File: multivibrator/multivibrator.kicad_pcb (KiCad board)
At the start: 2 copper layers, 11 parts, among them J1 Conn_01x02_Female, Q1 Q_NPN_BCE, Q2 Q_NPN_BCE

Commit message: improvement
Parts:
- J1: footprint Battery:BatteryHolder_Bulgin_BX0036_1xC -> Connector_PinHeader_2.54mm:PinHeader_1x02_P2.54mm_Vertical
- Q1, Q2: footprint Package_TO_SOT_THT:TO-92_HandSolder -> Package_TO_SOT_SMD:TSOT-23
- R1, R2, R3, R4: footprint Resistor_SMD:R_0201_0603Metric -> Resistor_SMD:R_1206_3216Metric
- moved J1 65.0 mm to (160.0, 88.9), turned to 0 degrees
- moved Q2 37.1 mm to (144.8, 96.5), turned to 90 degrees
- moved Q1 32.4 mm to (153.7, 96.5), turned to 270 degrees
- moved R4 31.0 mm to (151.1, 86.4), turned to 270 degrees
- moved C2 27.5 mm to (153.3, 91.4)
- moved D2 27.0 mm to (153.7, 82.5), turned to 90 degrees
- moved C1 25.8 mm to (145.7, 91.4)
- moved R1 25.0 mm to (143.5, 86.4), turned to 270 degrees
- moved R3 25.0 mm to (154.9, 86.4), turned to 270 degrees
- moved D1 24.5 mm to (145.8, 82.9), turned to 270 degrees
- moved R2 24.3 mm to (147.3, 86.4), turned to 270 degrees
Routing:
- net Net-(J1-Pad2): track 0.00 -> 52.4 mm
- net Net-(D1-Pad2): track 0.00 -> 28.2 mm
- net Net-(C1-Pad2): track 0.00 -> 24.8 mm
- net Net-(C2-Pad1): track 0.00 -> 14.2 mm
- net Net-(C1-Pad1): track 0.00 -> 12.3 mm
- net Net-(C2-Pad2): track 0.00 -> 8.85 mm
- net Net-(D1-Pad1): track 0.00 -> 3.68 mm
- net Net-(D2-Pad1): track 0.00 -> 3.41 mm
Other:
- rule pad_to_mask_clearance: 0.2 -> 0

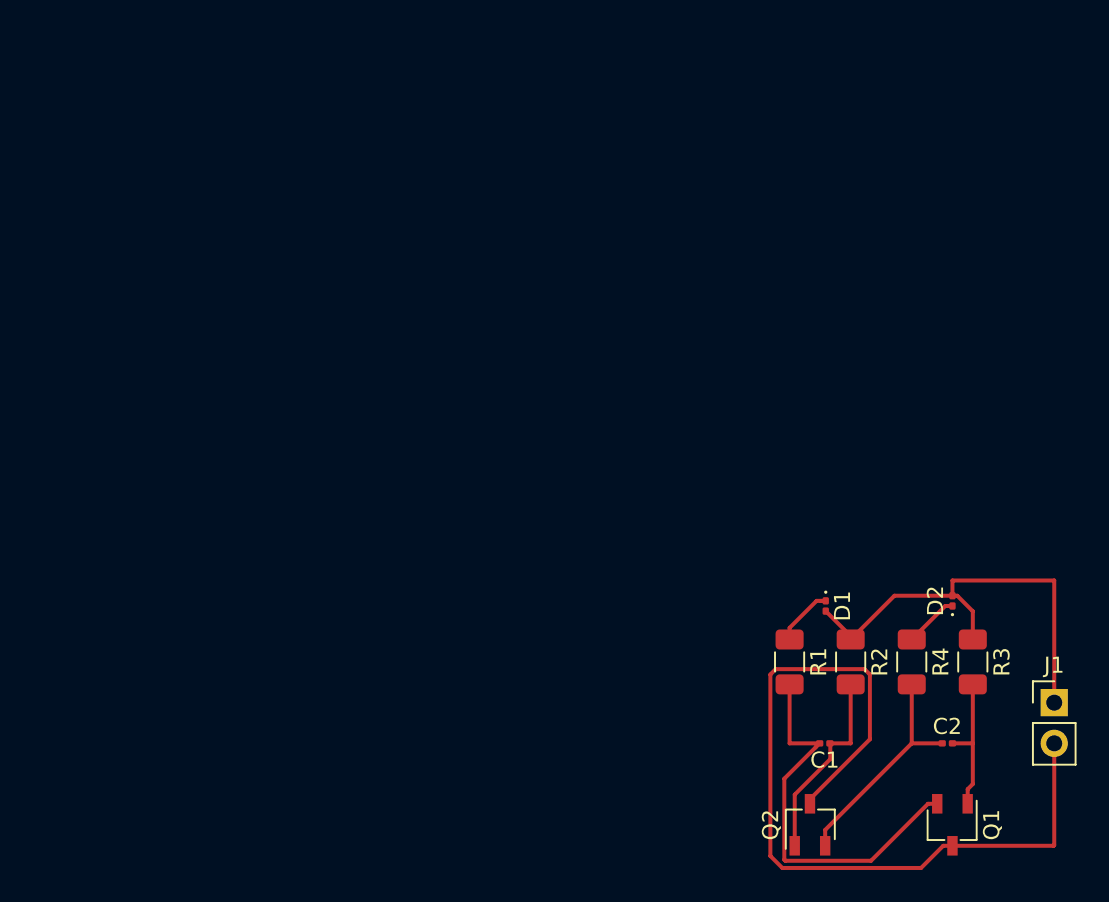
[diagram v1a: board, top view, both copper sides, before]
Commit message: review fixes, ready for print
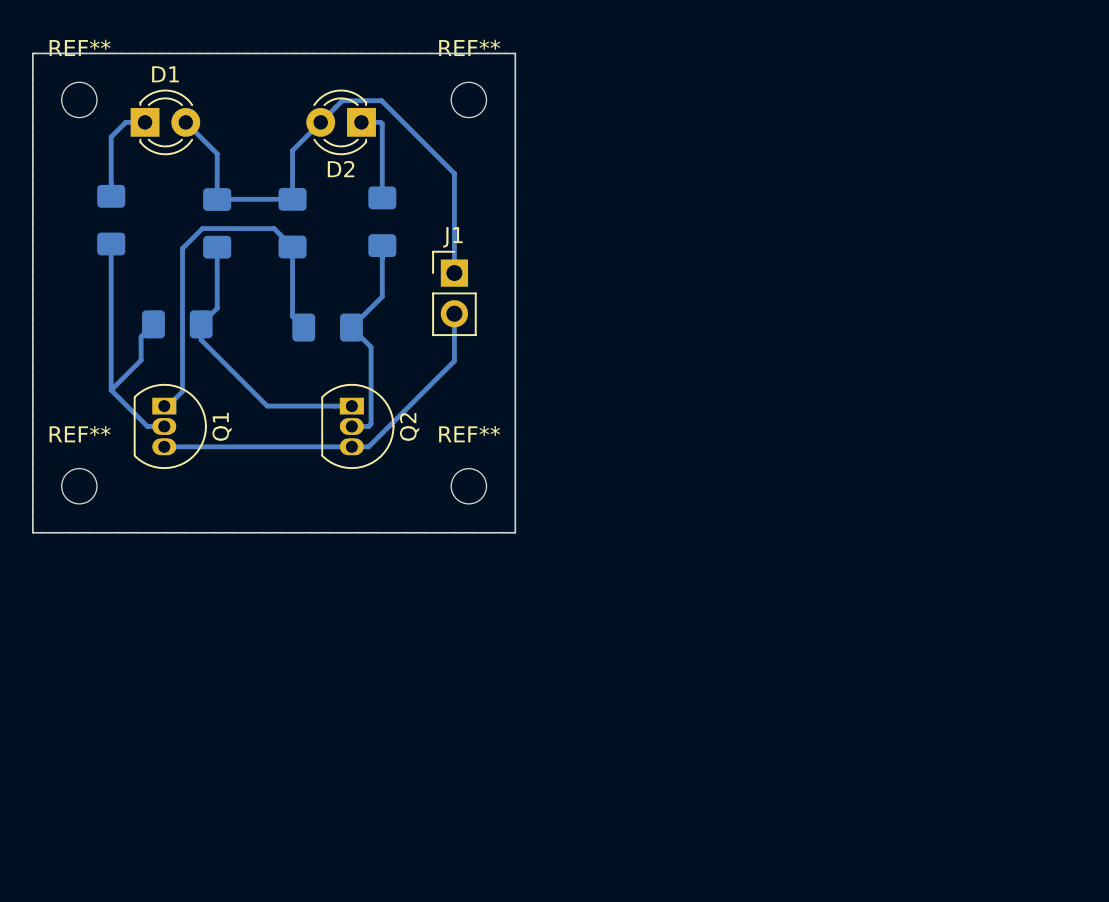
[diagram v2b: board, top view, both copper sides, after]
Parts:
- added REF**: MountingHole_2.2mm_M2, MountingHole:MountingHole_2.2mm_M2, F.Cu at (123.5, 51.3)
- added REF**: MountingHole_2.2mm_M2, MountingHole:MountingHole_2.2mm_M2, F.Cu at (99.2, 51.3)
- added REF**: MountingHole_2.2mm_M2, MountingHole:MountingHole_2.2mm_M2, F.Cu at (99.2, 75.4)
- added REF**: MountingHole_2.2mm_M2, MountingHole:MountingHole_2.2mm_M2, F.Cu at (123.5, 75.4)
- C1, C2: footprint Capacitor_SMD:C_0201_0603Metric -> Capacitor_SMD:C_1206_3216Metric_Pad1.42x1.75mm_HandSolder; moved to B.Cu
- D1, D2: footprint LED_SMD:LED_0201_0603Metric -> LED_THT:LED_D3.0mm
- Q1, Q2: footprint Package_TO_SOT_SMD:TSOT-23 -> Package_TO_SOT_THT:TO-92_Inline
- R1, R2, R3, R4: footprint Resistor_SMD:R_1206_3216Metric -> Resistor_SMD:R_1206_3216Metric_Pad1.42x1.75mm_HandSolder; moved to B.Cu
- moved Q1 55.7 mm to (104.5, 70.4)
- moved D1 52.1 mm to (103.3, 52.7), turned to 0 degrees
- moved R1 50.5 mm to (101.2, 58.8)
- moved R3 50.5 mm to (112.5, 59.0)
- moved C1 48.1 mm to (105.3, 65.3)
- moved R2 48.1 mm to (107.8, 59.0)
- moved D2 47.4 mm to (116.8, 52.7), turned to 180 degrees
- moved C2 46.6 mm to (114.7, 65.5), turned to 180 degrees
- moved J1 46.0 mm to (122.6, 62.1)
- moved R4 43.0 mm to (118.1, 58.9)
- moved Q2 38.7 mm to (116.2, 70.4), turned to 270 degrees
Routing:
- net Net-(J1-Pad2): track 52.4 -> 23.3 mm
- net Net-(C2-Pad2): track 8.85 -> 23.6 mm
- net Net-(C1-Pad2): track 24.8 -> 18.6 mm
- net Net-(C1-Pad1): track 12.3 -> 17.3 mm
- net Net-(D1-Pad2): track 28.2 -> 32.8 mm
- net Net-(D2-Pad1): track 3.41 -> 5.95 mm
- net Net-(D1-Pad1): track 3.68 -> 6.19 mm
- added copper zone on B.Cu, net Net-(J1-Pad2)
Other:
- board outline added: 30.1 x 29.9 mm
- net class Default: clearance 0.2 -> 0.3; trace_width 0.25 -> 0.3
- rule trace_clearance: 0.2 -> 0.3
